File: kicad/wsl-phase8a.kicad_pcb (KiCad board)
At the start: 2 copper layers, 41 parts, among them J1 5.08mm 2P TB, J10 5.08mm 2P TB, J11 5.08mm 2P TB, J2 5.08mm 2P TB, J3 5.08mm 2P TB, J4 5.08mm 2P TB, J5 5.08mm 2P TB, J6 5.08mm 2P TB, J7 5.08mm 2P TB, J8 5.08mm 2P TB, J9 5.08mm 2P TB, Q1 AO3400A, Q2 AO3400A, U1 NE555

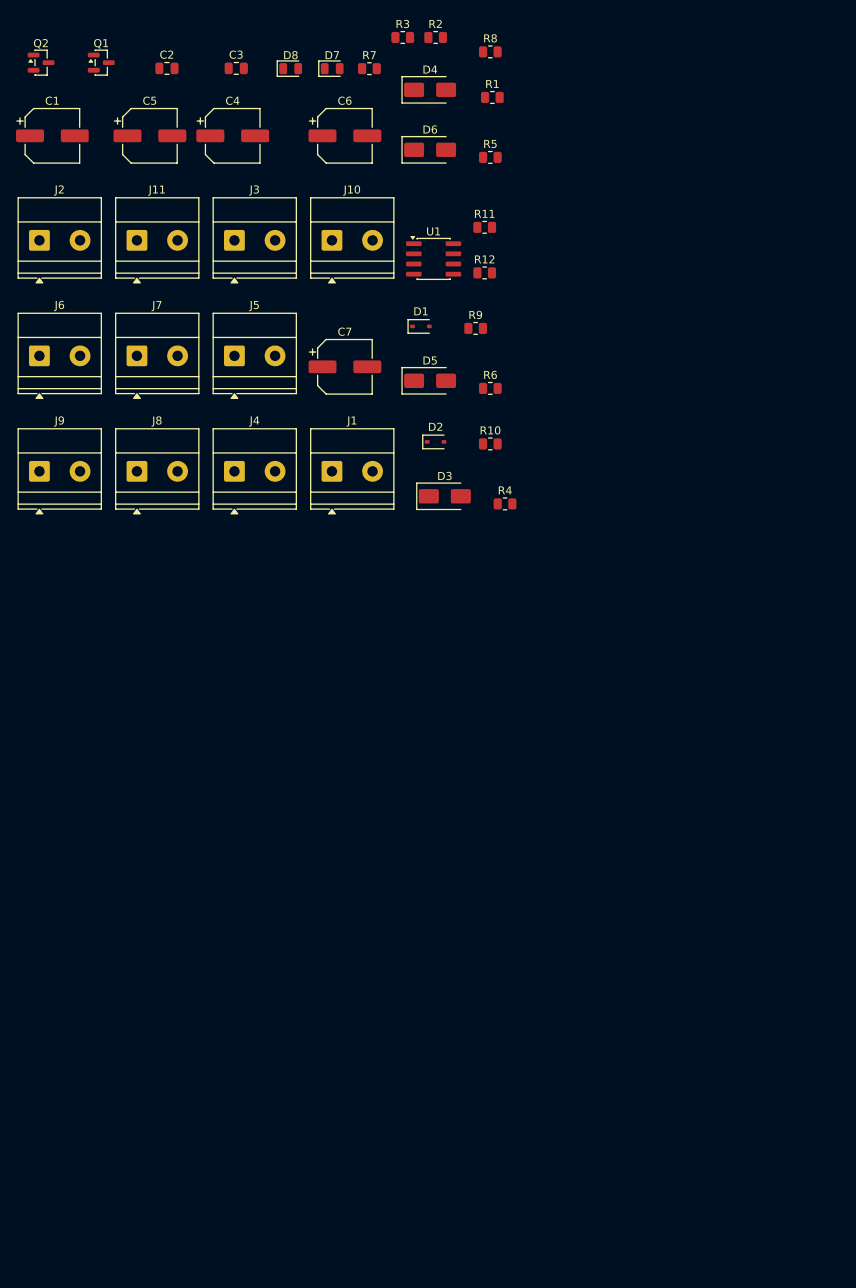
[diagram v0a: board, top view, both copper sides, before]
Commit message: Add programmatic placement script + placed board (post-KiCad-crash recovery)
KiCad crashed mid-DRC and lost ~45 min of manual placement work. Script
uses pcbnew Python API to place all 41 components at fixed coordinates
on a 100x100mm board: terminals around perimeter (J8-J11 top, J4-J7
bottom, J1-J3 left), watchdog cluster center-left interior, 4 AC
interposer channels stacked vertically on right interior. Edge.Cuts
board outline drawn programmatically too. Idempotent — safe to re-run
if placement needs adjustment.

Co-Authored-By: Claude Opus 4.7 (1M context) <noreply@anthropic.com>
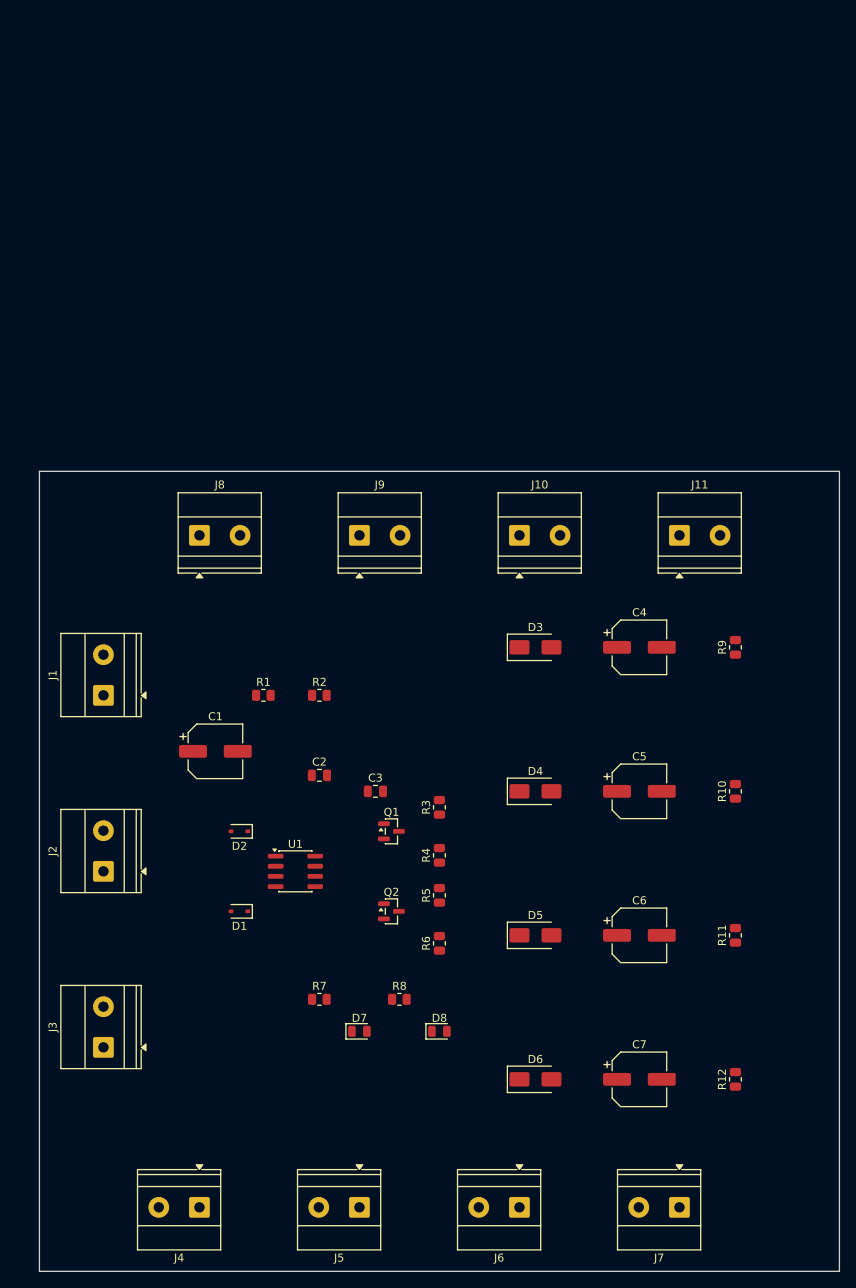
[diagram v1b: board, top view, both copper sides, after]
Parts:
- moved J7 126.2 mm to (80.0, 92.0), turned to 180 degrees
- moved J6 122.2 mm to (60.0, 92.0), turned to 180 degrees
- moved D8 121.8 mm to (50.0, 70.0)
- moved D7 120.4 mm to (40.0, 70.0)
- moved R8 119.0 mm to (45.0, 66.0)
- moved D6 116.9 mm to (62.0, 76.0)
- moved R7 116.5 mm to (35.0, 66.0)
- moved Q2 114.8 mm to (44.0, 55.0)
- moved J5 107.6 mm to (40.0, 92.0), turned to 180 degrees
- moved C6 106.5 mm to (75.0, 58.0)
- moved R12 105.6 mm to (87.0, 76.0), turned to 90 degrees
- moved Q1 102.7 mm to (44.0, 45.0)
- moved C5 102.3 mm to (75.0, 40.0)
- moved J3 102.2 mm to (8.00, 72.0), turned to 90 degrees
- moved C7 96.4 mm to (75.0, 76.0)
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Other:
- board outline added: 100 x 100 mm

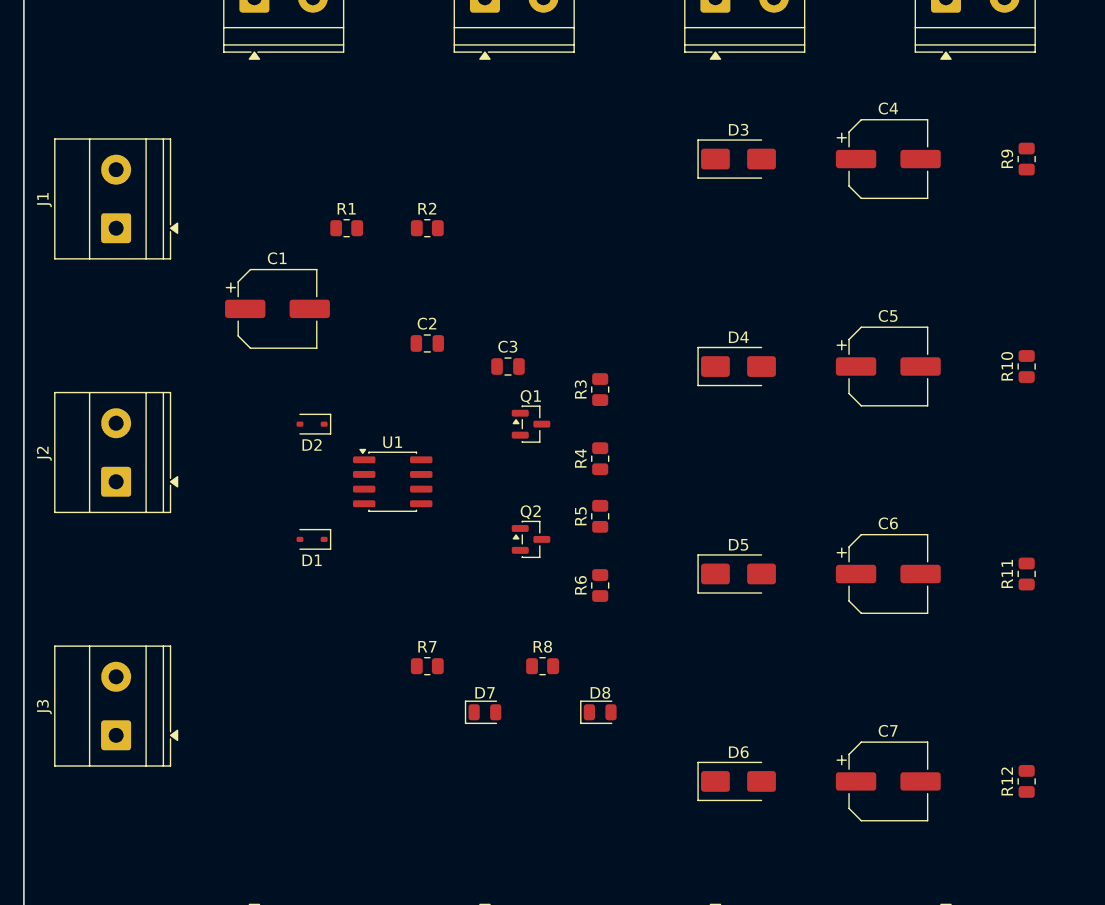
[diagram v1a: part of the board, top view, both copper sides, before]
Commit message: Optimize placement v2 — AC channels aligned with their terminals
Each AC channel is now a clean vertical column at the same x as its
DC_OUT and AC_IN terminals: ch1 at x=20, ch2 at x=40, ch3 at x=60,
ch4 at x=80. D (rectifier) at y=18 just below the DC_OUT terminal,
C (smoothing cap) at y=30, R (bleeder) at y=42. The 50mm vertical run
from R down to AC_IN at y=92 is a single straight trace per channel.

Watchdog cluster moved into the x-gaps between channel columns
(x≈10, 28, 48, 70) so channel return traces pass between watchdog
parts without collision. NE555 at x=32 between ch1/ch2 cols, MOSFETs
at x=52 between ch2/ch3, LEDs at x=76 between ch3/ch4.

Cuts the worst trace lengths from ~70mm diagonal to ~50mm straight
vertical.

Co-Authored-By: Claude Opus 4.7 (1M context) <noreply@anthropic.com>
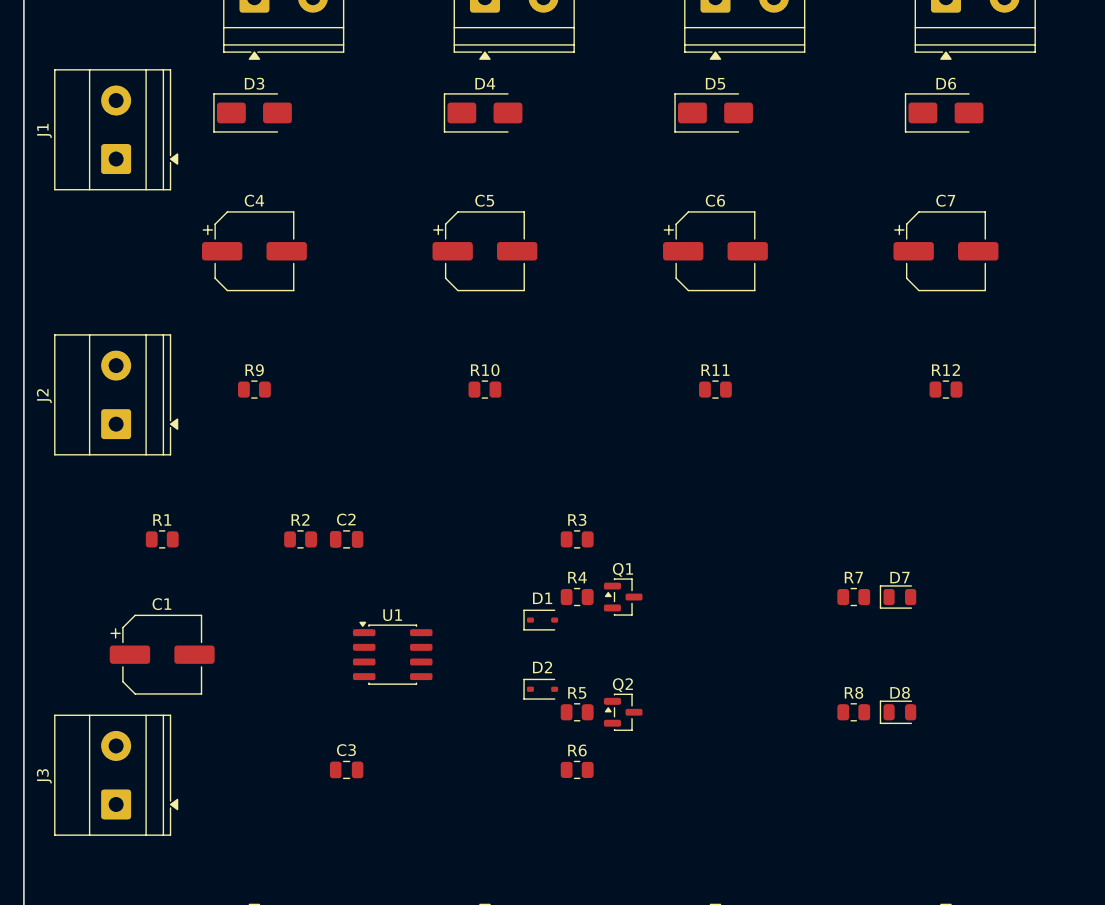
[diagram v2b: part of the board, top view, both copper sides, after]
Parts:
- moved R9 69.9 mm to (20.0, 42.0), turned to 0 degrees
- moved D6 60.7 mm to (80.0, 18.0)
- moved C4 55.6 mm to (20.0, 30.0)
- moved R10 47.0 mm to (40.0, 42.0), turned to 0 degrees
- moved C7 46.3 mm to (80.0, 30.0)
- moved D3 42.2 mm to (20.0, 18.0)
- moved D5 40.0 mm to (60.0, 18.0)
- moved C3 37.7 mm to (28.0, 75.0)
- moved R7 37.5 mm to (72.0, 60.0)
- moved D7 37.4 mm to (76.0, 60.0)
- moved C5 36.4 mm to (40.0, 30.0)
- moved R12 34.7 mm to (80.0, 42.0), turned to 0 degrees
- moved C6 31.8 mm to (60.0, 30.0)
- moved C1 31.6 mm to (12.0, 65.0)
- moved R1 31.4 mm to (12.0, 55.0)
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
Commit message: Apply Codex rev A audit fixes: D_PROT, 63V caps, mounting holes
Three pre-route critical fixes from external review:

1. AC interposer caps C4-C7: 10uF/50V -> 10uF/63V.
   Field signal can hit ~32V RMS = ~45V peak before transients; 50V
   was operating at the edge. 63V gives proper headroom.

2. Reverse-polarity protection on +5V input.
   New D_PROT (SS14 Schottky, SMA) between J1 raw input and the rest
   of VCC_5V. Series diode opens if +5V/GND are swapped at install.
   ~0.3V forward drop means downstream rail is 4.7V — within AEDIKO
   and NE555 operating range. SKiDL assigns refdes D9 (after the 8
   existing diode-prefix parts).

3. M3 mounting holes at 4 corners.
   3.2mm NPTH at (3.5, 3.5), (96.5, 3.5), (3.5, 96.5), (96.5, 96.5).
   Refdes MK1-MK4. Added programmatically via place_components.py.

Deferred to rev B per Codex notes that don't block fab:
- Test pads for key signals (useful but not blocking)
- Silkscreen field labels (will add before final fab)
- Tighter U1 timing-network placement (1Hz/11s timing is insensitive
  to ~20mm trace stray capacitance)

Co-Authored-By: Claude Opus 4.7 (1M context) <noreply@anthropic.com>
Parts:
- added D9: SS14, Diode_SMD:D_SMA, F.Cu at (16.0, 33.0)
- added MK1: MountingHole_3.2mm_M3, MountingHole_3.2mm_M3, F.Cu at (3.50, 3.50)
- added MK2: MountingHole_3.2mm_M3, MountingHole_3.2mm_M3, F.Cu at (96.5, 3.50)
- added MK3: MountingHole_3.2mm_M3, MountingHole_3.2mm_M3, F.Cu at (3.50, 96.5)
- added MK4: MountingHole_3.2mm_M3, MountingHole_3.2mm_M3, F.Cu at (96.5, 96.5)
- C4, C5, C6, C7: value 10uF/50V -> 10uF/63V
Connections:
- J1 pad 1: VCC_5V -> VCC_5V_RAW

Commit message: Add test pads + silkscreen labels (rev A audit pass 2)
Codex's second-pass review wanted test pads and field-service silkscreen
labels. Cherry-picked those additions (not Codex's whole script — that
had two real bugs: J2/J3 vertical overlap and U1/C5 body collision).

14 test pads added:
  TP1-TP6: VCC_5V, GND, KICK, TIMING_NODE, NE555_OUT, COIL_GND_RETURN
  TP7-TP14: DC_CHx_POS + CHx_RETURN for each of 4 AC channels

1.5mm round SMD pads on F.Cu with F.Mask aperture (exposed copper for
probing). Created programmatically as single-pad footprints.

18 silkscreen labels on F.Silkscreen:
  - Power terminals: +5V/GND, AEDIKO V+/V-, KICK/GND
  - DC OUT (top): CH1-4 DC OUT
  - AC IN (bottom): CH1-4 24VAC
  - Indicator LEDs: WD, PWR
  - Service note: "T_OUT ~11s" near NE555
  - Title: "WSL Phase 8a Rev A"

Total board population now: 42 components + 4 mounting holes + 14 test
pads + 18 silkscreen text items = 60 placed items.

Co-Authored-By: Claude Opus 4.7 (1M context) <noreply@anthropic.com>
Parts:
- added TP1: VCC_5V, , F.Cu at (25.0, 22.0)
- added TP10: CH2_RETURN, , F.Cu at (46.0, 36.0)
- added TP11: DC_CH3_POS, , F.Cu at (54.0, 36.0)
- added TP12: CH3_RETURN, , F.Cu at (66.0, 36.0)
- added TP13: DC_CH4_POS, , F.Cu at (74.0, 36.0)
- added TP14: CH4_RETURN, , F.Cu at (86.0, 36.0)
- added TP2: GND, , F.Cu at (25.0, 28.0)
- added TP3: KICK, , F.Cu at (18.0, 80.0)
- added TP4: TIMING_NODE, , F.Cu at (6.00, 60.0)
- added TP5: NE555_OUT, , F.Cu at (40.0, 65.0)
- added TP6: COIL_GND_RETURN, , F.Cu at (58.0, 70.0)
- added TP7: DC_CH1_POS, , F.Cu at (14.0, 36.0)
- added TP8: CH1_RETURN, , F.Cu at (26.0, 36.0)
- added TP9: DC_CH2_POS, , F.Cu at (34.0, 36.0)
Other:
- board text added: "+5V"
- board text added: "AEDIKO V+"
- board text added: "AEDIKO V-"
- board text added: "CH1 24VAC"
- board text added: "CH1 DC OUT"
- board text added: "CH2 24VAC"
- board text added: "CH2 DC OUT"
- board text added: "CH3 24VAC"
- board text added: "CH3 DC OUT"
- board text added: "CH4 24VAC"
- board text added: "CH4 DC OUT"
- board text added: "GND"
- board text added: "KICK"
- board text added: "PWR"
- board text added: "T_OUT ~11s"
- board text added: "WD"
- board text added: "WSL Phase 8a Rev A"

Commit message: Rev A polish per Codex pass 3: tighter timing cluster + shorter labels
- C1 (timing cap) moved from (12, 65) to (30, 58): directly above
  U1.7/U1.6 (THRES/DISCH). TIMING_NODE trace now ~7mm vs ~20mm prior.
- C2 (VCC bypass) moved from (28, 55) to (28, 65): hugging U1.8 (VCC)
  and U1.1 (GND), 0.5mm from U1 body left edge.
- C3 (CTRL filter) moved from (28, 75) to (37, 60): right of U1.5
  (CTRL) for short bypass-to-GND path.
- R1 (timing pullup) moved from (12, 55) to (32, 52): directly above
  C1, TIMING_NODE pullup loop stays compact.
- R2 (TRIG pullup) moved from (24, 55) to (25, 67): left of U1.2 (TRIG).
- D9 (SS14 reverse-polarity) moved from (16, 33) to (15, 22):
  immediately right of J1, VCC_5V_RAW reduced to <3mm long.

Silkscreen labels: replaced "CH1 DC OUT" / "CH1 24VAC" (long, overlapping
the channel diodes/resistors) with per-pin short labels DC1+/DC1-/AC1
L1/AC1 L2. Labels now fit in the narrow gap between connectors and
adjacent components without overlap.

Polarity verified by netlist construction (no script change needed):
  D3-D6 (M7): pin1=K -> DC_CHx_POS, pin2=A -> AC_CHx_L1
  C4-C7 (CP): pin1=+ -> DC_CHx_POS, pin2=- -> CHx_RETURN
  D9 (SS14): pin1=K -> VCC_5V (protected), pin2=A -> VCC_5V_RAW

Co-Authored-By: Claude Opus 4.7 (1M context) <noreply@anthropic.com>
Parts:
- moved R1 20.2 mm to (32.0, 52.0)
- moved C1 19.3 mm to (30.0, 58.0)
- moved C3 17.5 mm to (37.0, 60.0)
- moved R2 12.0 mm to (25.0, 67.0)
- moved D9 11.0 mm to (15.0, 22.0)
- moved C2 10.0 mm to (28.0, 65.0)
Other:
- board text added: "AC1 L1"
- board text added: "AC1 L2"
- board text added: "AC2 L1"
- board text added: "AC2 L2"
- board text added: "AC3 L1"
- board text added: "AC3 L2"
- board text added: "AC4 L1"
- board text added: "AC4 L2"
- board text added: "DC1+"
- board text added: "DC1-"
- board text added: "DC2+"
- board text added: "DC2-"
- board text added: "DC3+"
- board text added: "DC3-"
- board text added: "DC4+"
- board text added: "DC4-"
- board text removed: "CH1 24VAC"
- board text removed: "CH1 DC OUT"
- board text removed: "CH2 24VAC"
- board text removed: "CH2 DC OUT"
- board text removed: "CH3 24VAC"
- board text removed: "CH3 DC OUT"
- board text removed: "CH4 24VAC"
- board text removed: "CH4 DC OUT"
